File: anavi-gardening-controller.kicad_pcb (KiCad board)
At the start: 2 copper layers, 57.7 x 47.2 mm, 19 parts, among them J1 Conn_01x04_Female, J2 Conn_01x04_Female, J3 Conn_01x04_Female, J4 Conn_01x04_Female, J5 Conn_02x04_Odd_Even, U1 MOUDLE-SEEEDUINO-XIAO-ESP32C3, U2 DS18B20

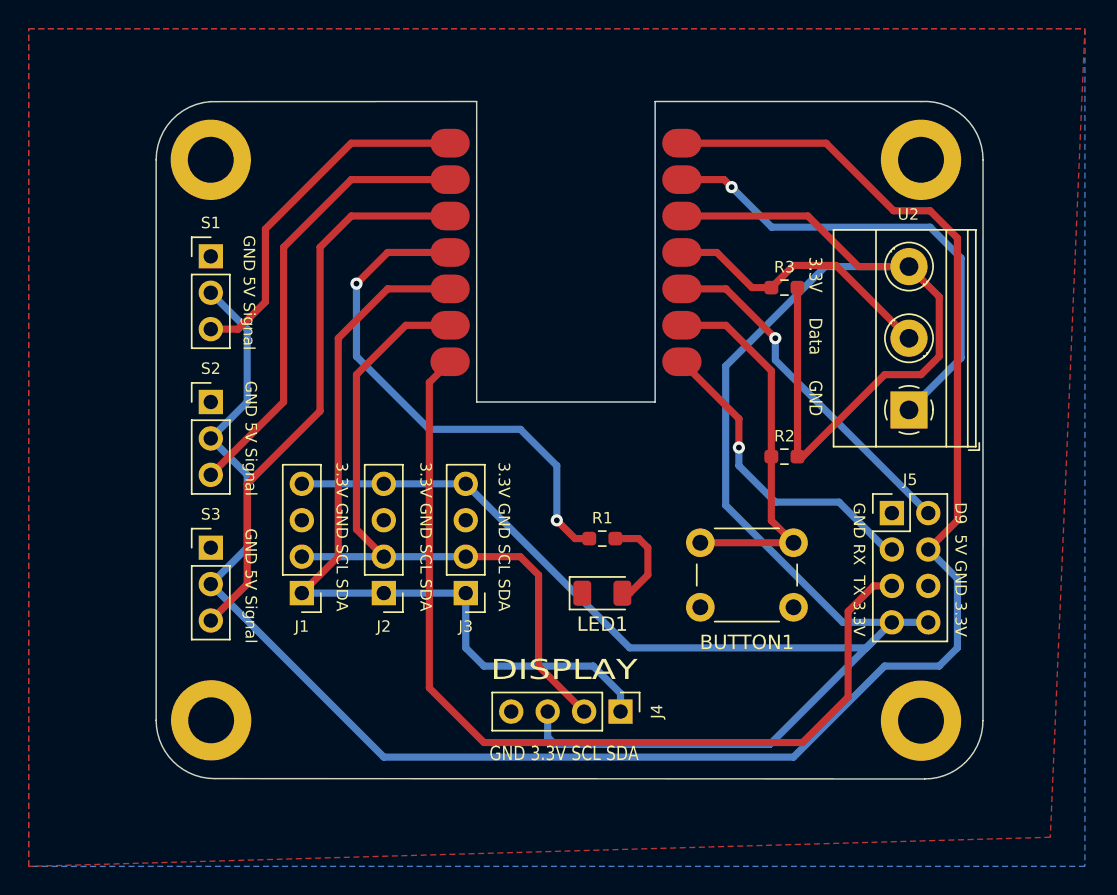
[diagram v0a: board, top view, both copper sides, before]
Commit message: Update silkscreen
Add logo and text to the front and the back silkscreen.

Signed-off-by: Leon Anavi <leon@anavi.org>
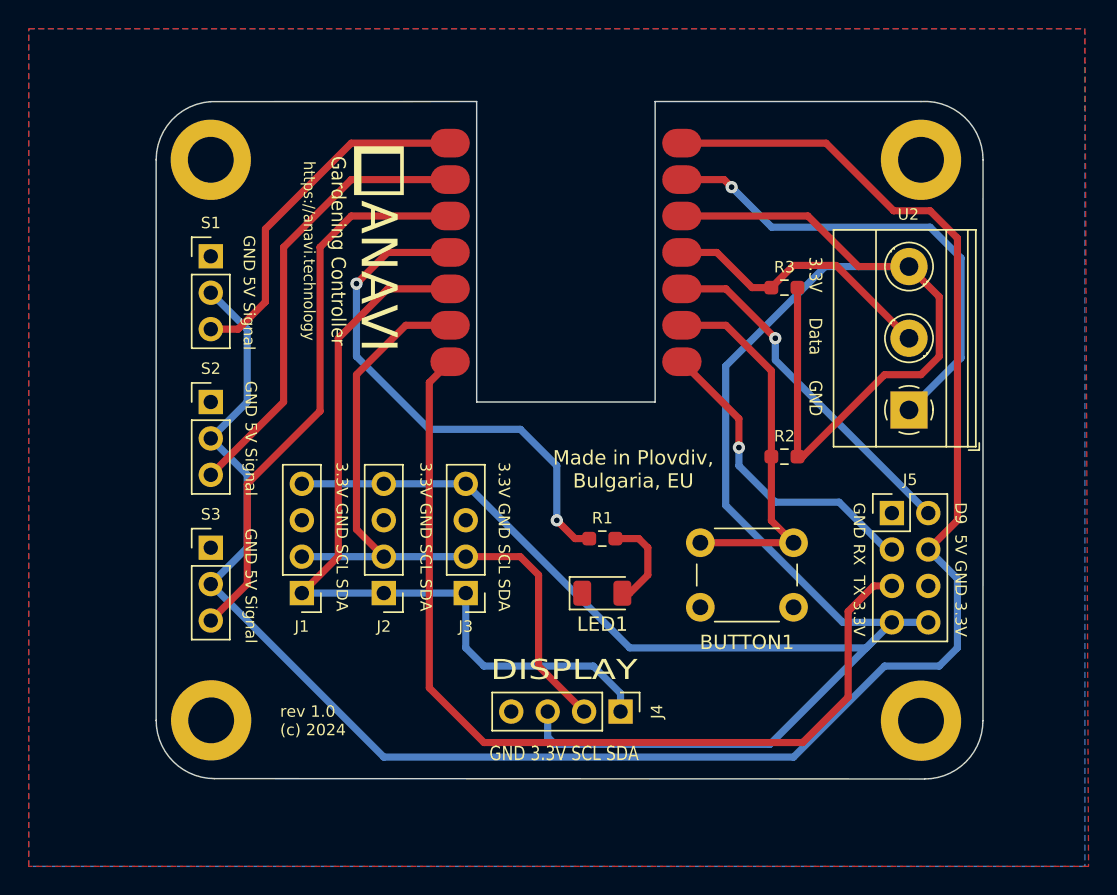
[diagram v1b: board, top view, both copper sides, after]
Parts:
- added G***: LOGO, logo:anavi-logo, F.Cu at (136.1, 37.8)
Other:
- board text added: ":)"
- board text added: "ANAVI"
- board text added: "Gardening Controller"
- board text added: "Made in Plovdiv, Bulgaria, EU"
- board text added: "Open source hardware gives people the freedom to control their technology."
- board text added: "Plug your plants into the digital conversation!"
- board text added: "https://anavi.technology"
- board text added: "rev 1.0 (c) 2024"
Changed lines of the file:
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@@
     (pad "2" thru_hole circle (at 0 0) (size 5.6 5.6) (drill 3.2) (layers *.Cu *.Mask))
+  )
+  (footprint "logo:anavi-logo" (layer "F.Cu")
+    (at 136.144 37.846 -90)
+    (attr through_hole)
+    (fp_text reference "G***" (at 0 0 90) (layer "F.SilkS") hide
+      (effects (font (size 1.524 1.524) (thickness 0.3)))
+    )
+    (fp_text value "LOGO" (at 0.75 0 90) (layer "F.SilkS") hide
+      (effects (font (size 1.524 1.524) (thickness 0.3)))
+    )
+    (fp_poly (pts
+        (xy 1.693334 1.693334)
+        (xy -1.693333 1.693334)
+        (xy -1.693333 -1.524)
+        (xy -1.185333 -1.524)
+        (xy -1.185333 1.185334)
+        (xy 1.439334 1.185334)
+        (xy 1.439334 -1.524)
+        (xy -1.185333 -1.524)
+        (xy -1.693333 -1.524)
+        (xy -1.693333 -1.778)
+        (xy 1.693334 -1.778)
+        (xy 1.693334 1.693334)
+      ) (layer "F.SilkS") (width 0.01) (fill solid))
   )
   (footprint "MountingHole:MountingHole_3.2mm_M3_DIN965_Pad" (layer "F.Cu")
@@
   (gr_line (start 120.65 76.1746) (end 120.65 37.084) (layer "Edge.Cuts") (width 0.1))
   (gr_line (start 143.002 33.02) (end 143.002 53.975) (layer "Edge.Cuts") (width 0.1))
+  (gr_text "Plug your plants into\nthe digital conversation!" (at 131.318 45.72 270) (layer "B.SilkS")
+    (effects (font (size 1 1) (thickness 0.15)) (justify mirror))
+  )
+  (gr_text "Open source hardware gives people the\nfreedom to control their technology." (at 166.116 48.006 270) (layer "B.SilkS")
+    (effects (font (size 0.8 0.8) (thickness 0.12)) (justify mirror))
+  )
+  (gr_text ":)" (at 137.414 44.958) (layer "B.SilkS")
+    (effects (font (size 1.8 1.8) (thickness 0.2)) (justify mirror))
+  )
+  (gr_text "Gardening Controller" (at 133.35 43.434 270) (layer "F.SilkS")
+    (effects (font (size 1 0.92) (thickness 0.15)))
+  )
   (gr_text "3.3V GND SCL SDA" (at 133.604 63.373 -90) (layer "F.SilkS")
     (effects (font (size 0.8 0.8) (thickness 0.15)))
   )
+  (gr_text "rev 1.0\n(c) 2024" (at 129.286 76.2) (layer "F.SilkS")
+    (effects (font (size 0.8 0.8) (thickness 0.12)) (justify left))
+  )
   (gr_text "GND 5V Signal" (at 127.254 56.515 -90) (layer "F.SilkS")
     (effects (font (size 0.8 0.8) (thickness 0.15)))
@@
   (gr_text "GND 5V Signal" (at 127.127 46.355 -90) (layer "F.SilkS")
     (effects (font (size 0.8 0.8) (thickness 0.15)))
+  )
+  (gr_text "https://anavi.technology" (at 131.318 43.434 270) (layer "F.SilkS")
+    (effects (font (size 0.8 0.75) (thickness 0.12)))
   )
   (gr_text "3.3V GND SCL SDA" (at 139.446 63.373 -90) (layer "F.SilkS")
@@
     (effects (font (size 0.8 0.8) (thickness 0.1)))
   )
+  (gr_text "ANAVI" (at 136.144 45.212 270) (layer "F.SilkS")
+    (effects (font (size 2.5 2.5) (thickness 0.4)))
+  )
   (gr_text "D9  5V GND 3.3V" (at 176.7586 65.659 -90) (layer "F.SilkS")
     (effects (font (size 0.8 0.8) (thickness 0.1)))
@@
   (gr_text "3.3V GND SCL SDA" (at 144.907 63.373 -90) (layer "F.SilkS")
     (effects (font (size 0.8 0.8) (thickness 0.15)))
+  )
+  (gr_text "Made in Plovdiv,\nBulgaria, EU" (at 153.924 58.674) (layer "F.SilkS")
+    (effects (font (size 1 1) (thickness 0.15)))
   )
   (gr_text "DISPLAY" (at 149.098 72.644) (layer "F.SilkS")
@@
     (polygon
       (pts
-        (xy 183.007 84.328)
+        (xy 185.674 86.36)
         (xy 111.76 86.36)
         (xy 111.76 27.94)
